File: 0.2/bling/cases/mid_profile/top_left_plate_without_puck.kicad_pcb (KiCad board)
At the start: 2 copper layers, 110.3 x 98 mm, 0 parts

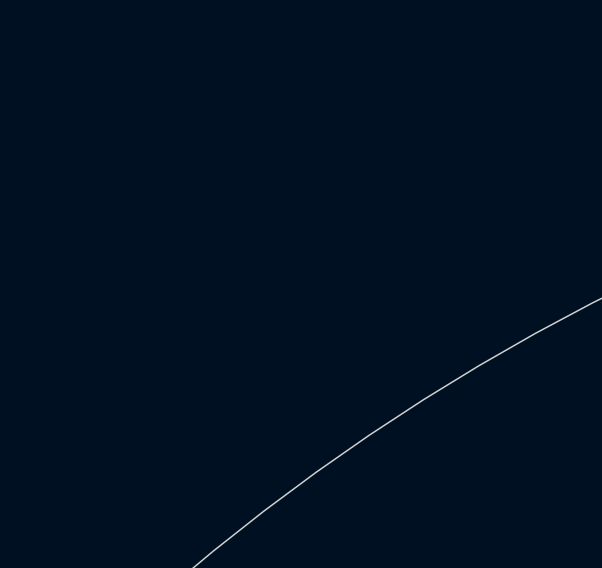
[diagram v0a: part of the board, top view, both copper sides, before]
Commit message: Add dummy component to each plate case
This works around a segfault in Pcbdraw which prevents renders in the
edge case where a PCB file has no module.
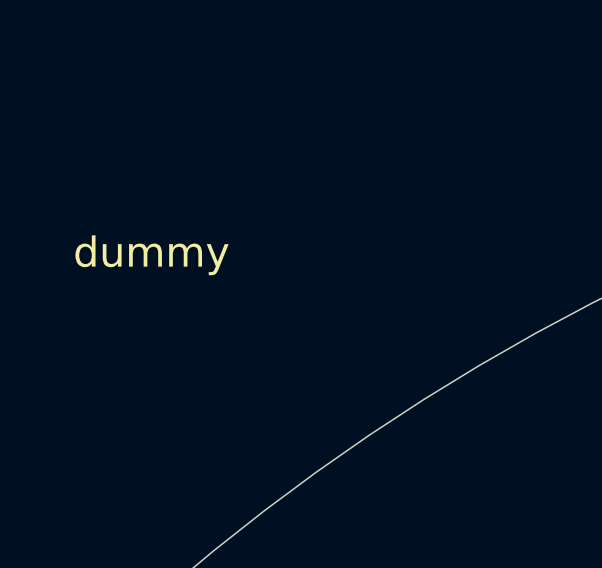
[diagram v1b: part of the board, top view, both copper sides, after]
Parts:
- added dummy: dummy, dummy:dummy, F.Cu at (12.0, 12.0)
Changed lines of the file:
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@@
     (tracks 0)
     (zones 0)
-    (modules 0)
+    (modules 1)
     (nets 1)
   )
@@
     (uvia_drill 0.1)
   )
+  (module dummy:dummy (layer F.Cu)
+    (at 12 12)
+    (fp_text reference dummy (at 0 0.5) (layer F.SilkS)
+      (effects (font (size 1 1) (thickness 0.15)))
+    )
+    (fp_text value dummy (at 0 -0.5) (layer F.Fab)
+      (effects (font (size 1 1) (thickness 0.15)))
+    )
+  )
   (gr_line (start 69 68.5) (end 69 54.5) (layer Edge.Cuts) (width 0.05))

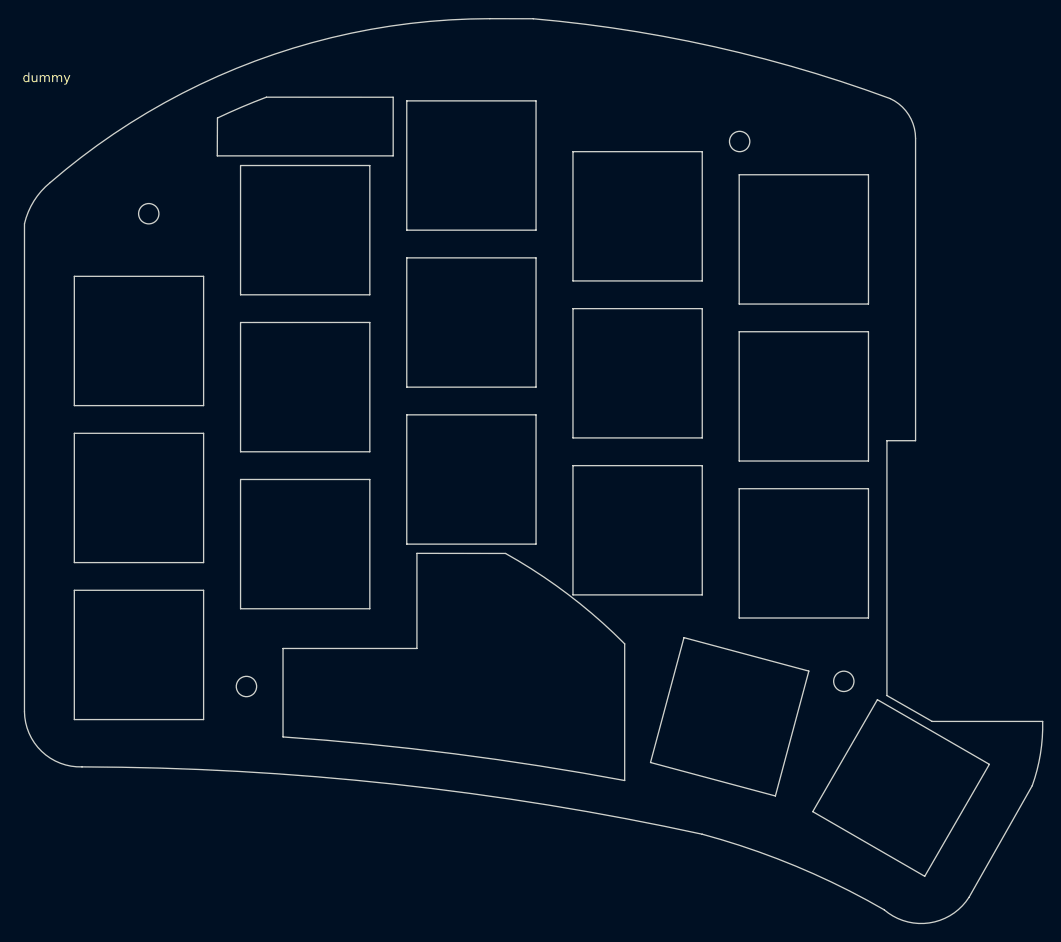
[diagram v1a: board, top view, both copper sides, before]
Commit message: Bling case: make thinnest places a bit thicker
One of the samples I received was damaged in one of the thin points.
In person, I could see that there was a little bit of margin to make
the design a bit more solid.
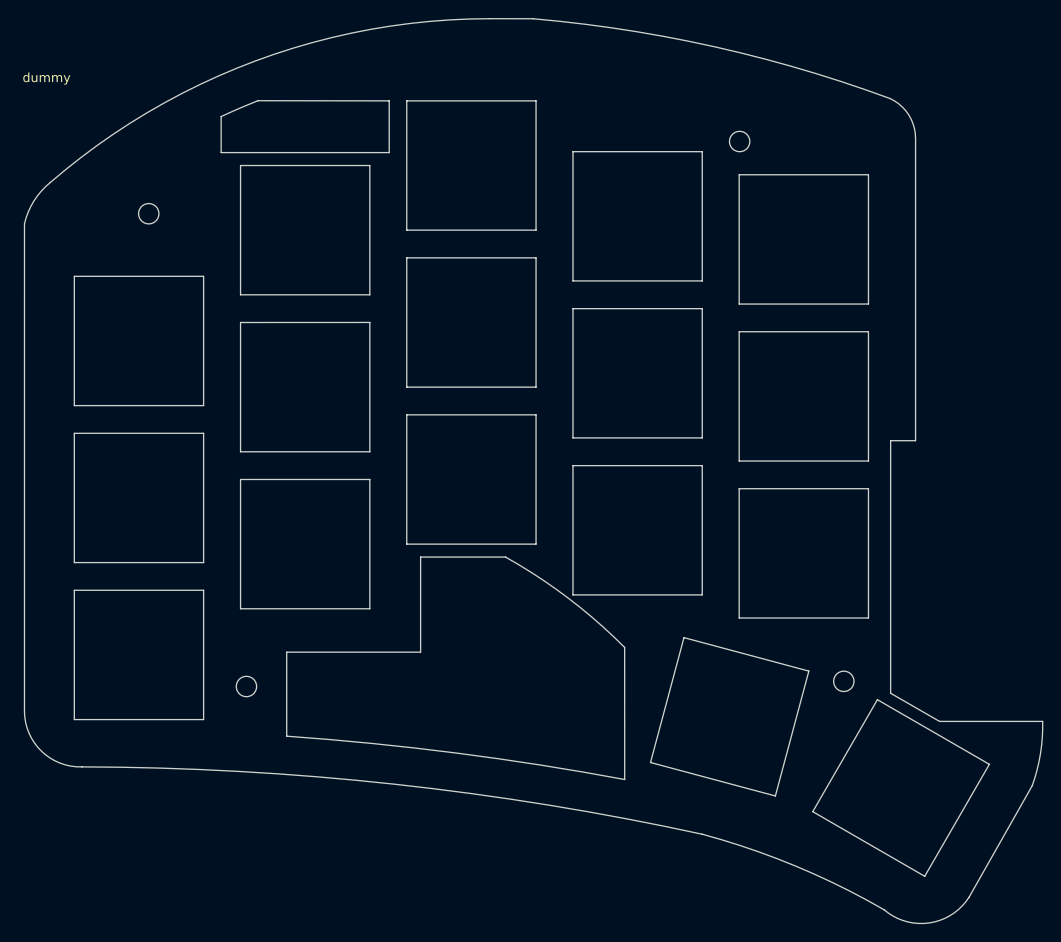
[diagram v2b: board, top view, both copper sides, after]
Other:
- outline, holes or cut-outs redrawn
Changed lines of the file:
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@@
     )
   )
-  (gr_line (start 69 68.5) (end 69 54.5) (layer Edge.Cuts) (width 0.05))
   (gr_line (start 107.092178 98.972178) (end 94.967822 91.972178) (layer Edge.Cuts) (width 0.05))
   (gr_line (start 114.092178 86.847822) (end 107.092178 98.972178) (layer Edge.Cuts) (width 0.05))
@@
   (gr_line (start 29 34) (end 29 48) (layer Edge.Cuts) (width 0.05))
   (gr_line (start 15 34) (end 29 34) (layer Edge.Cuts) (width 0.05))
-  (gr_line (start 69 34.5) (end 69 20.5) (layer Edge.Cuts) (width 0.05))
+  (gr_line (start 69 34.5) (end 69 20.499999) (layer Edge.Cuts) (width 0.05))
   (gr_line (start 83 34.5) (end 69 34.5) (layer Edge.Cuts) (width 0.05))
   (gr_line (start 83 20.5) (end 83 34.5) (layer Edge.Cuts) (width 0.05))
-  (gr_line (start 69 20.5) (end 83 20.5) (layer Edge.Cuts) (width 0.05))
-  (gr_line (start 87 23) (end 87 37) (layer Edge.Cuts) (width 0.05))
+  (gr_line (start 69 20.499999) (end 83 20.5) (layer Edge.Cuts) (width 0.05))
+  (gr_line (start 87 23) (end 87 37.001657) (layer Edge.Cuts) (width 0.05))
   (gr_line (start 101 23) (end 87 23) (layer Edge.Cuts) (width 0.05))
   (gr_line (start 101 37) (end 101 23) (layer Edge.Cuts) (width 0.05))
-  (gr_line (start 87 37) (end 101 37) (layer Edge.Cuts) (width 0.05))
+  (gr_line (start 87 37.001657) (end 101 37) (layer Edge.Cuts) (width 0.05))
   (gr_line (start 101 40) (end 87 40) (layer Edge.Cuts) (width 0.05))
   (gr_line (start 101 54) (end 101 40) (layer Edge.Cuts) (width 0.05))
@@
   (gr_line (start 83 68.5) (end 83 54.5) (layer Edge.Cuts) (width 0.05))
   (gr_line (start 69 68.5) (end 83 68.5) (layer Edge.Cuts) (width 0.05))
+  (gr_line (start 69 54.5) (end 69 68.5) (layer Edge.Cuts) (width 0.05))
   (gr_line (start 47 53) (end 47 38.995673) (layer Edge.Cuts) (width 0.05))
   (gr_line (start 33 53) (end 47 53) (layer Edge.Cuts) (width 0.05))
@@
   (gr_circle (center 33.639819 78.42) (end 34.739819 78.44) (layer Edge.Cuts) (width 0.05))
   (gr_circle (center 23.059819 27.22) (end 24.159819 27.24) (layer Edge.Cuts) (width 0.05))
-  (gr_arc (start 33.105131 115.090834) (end 74.6 73.8) (angle -15.90604465) (layer Edge.Cuts) (width 0.05))
-  (gr_arc (start 60.008389 78.858139) (end 35.8 14.6) (angle -4.807870918) (layer Edge.Cuts) (width 0.05))
+  (gr_arc (start 33.101375 115.479917) (end 74.596244 74.189083) (angle -15.90183156) (layer Edge.Cuts) (width 0.05))
+  (gr_arc (start 60.007609 78.856472) (end 34.89183 14.982553) (angle -3.628308496) (layer Edge.Cuts) (width 0.05))
   (gr_line (start 118.738448 89.155884) (end 111.890143 101.245816) (layer Edge.Cuts) (width 0.05))
   (gr_arc (start 106.708 97.938735) (end 102.7 102.6) (angle -98.1305031) (layer Edge.Cuts) (width 0.05))
@@
   (gr_line (start 64.699364 6.107346) (end 60 6.1) (layer Edge.Cuts) (width 0.05))
   (gr_arc (start 100.5318 82.63446) (end 118.738448 89.155884) (angle -20.9939576) (layer Edge.Cuts) (width 0.05))
-  (gr_line (start 107.9 82.2) (end 119.866285 82.200094) (layer Edge.Cuts) (width 0.05))
-  (gr_line (start 103 79.4) (end 107.9 82.2) (layer Edge.Cuts) (width 0.05))
-  (gr_line (start 103 51.8) (end 103 79.4) (layer Edge.Cuts) (width 0.05))
-  (gr_line (start 106.1 51.8) (end 103 51.8) (layer Edge.Cuts) (width 0.05))
+  (gr_line (start 108.7 82.2) (end 119.866285 82.200094) (layer Edge.Cuts) (width 0.05))
+  (gr_line (start 103.4 79.15) (end 108.7 82.2) (layer Edge.Cuts) (width 0.05))
+  (gr_line (start 103.4 51.8) (end 103.4 79.15) (layer Edge.Cuts) (width 0.05))
+  (gr_line (start 106.1 51.8) (end 103.4 51.8) (layer Edge.Cuts) (width 0.05))
   (gr_arc (start 51.873581 154.194988) (end 103.34992 14.75096) (angle -15.311832) (layer Edge.Cuts) (width 0.05))
   (gr_line (start 106.1 51.8) (end 106.1 19.059419) (layer Edge.Cuts) (width 0.05))
-  (gr_arc (start 15.142431 407.353485) (end 74.6 88.6) (angle -6.594680347) (layer Edge.Cuts) (width 0.05))
-  (gr_line (start 52.1 64) (end 61.695067 64.008815) (layer Edge.Cuts) (width 0.05))
-  (gr_line (start 52.1 74.3) (end 52.1 64) (layer Edge.Cuts) (width 0.05))
-  (gr_line (start 37.6 74.3) (end 52.1 74.3) (layer Edge.Cuts) (width 0.05))
-  (gr_line (start 37.599377 83.880654) (end 37.6 74.3) (layer Edge.Cuts) (width 0.05))
-  (gr_line (start 74.6 73.8) (end 74.6 88.6) (layer Edge.Cuts) (width 0.05))
-  (gr_line (start 30.499402 16.855121) (end 30.48 20.955) (layer Edge.Cuts) (width 0.05))
-  (gr_line (start 49.53 14.605) (end 35.8 14.6) (layer Edge.Cuts) (width 0.05))
-  (gr_line (start 49.53 20.955) (end 49.53 14.605) (layer Edge.Cuts) (width 0.05))
-  (gr_line (start 30.48 20.955) (end 49.53 20.955) (layer Edge.Cuts) (width 0.05))
+  (gr_arc (start 15.143653 407.236195) (end 74.600609 88.491383) (angle -6.523999184) (layer Edge.Cuts) (width 0.05))
+  (gr_line (start 52.5 64.4) (end 61.695067 64.4) (layer Edge.Cuts) (width 0.05))
+  (gr_line (start 52.5 74.7) (end 52.5 64.4) (layer Edge.Cuts) (width 0.05))
+  (gr_line (start 38 74.7) (end 52.5 74.7) (layer Edge.Cuts) (width 0.05))
+  (gr_line (start 38 83.8) (end 38 74.7) (layer Edge.Cuts) (width 0.05))
+  (gr_line (start 74.596244 74.189083) (end 74.600609 88.491383) (layer Edge.Cuts) (width 0.05))
+  (gr_line (start 30.9 16.7) (end 30.9 20.6) (layer Edge.Cuts) (width 0.05))
+  (gr_line (start 49.1 15) (end 34.89183 14.982553) (layer Edge.Cuts) (width 0.05))
+  (gr_line (start 49.1 20.6) (end 49.1 15) (layer Edge.Cuts) (width 0.05))
+  (gr_line (start 30.9 20.6) (end 49.1 20.6) (layer Edge.Cuts) (width 0.05))
   (gr_arc (start 17.48 30.13) (end 15.035 26.885) (angle -35.4) (layer Cmts.User) (width 0.05))
   (gr_line (start 102.1 49.9) (end 102.1 19.059419) (layer Cmts.User) (width 0.05))
